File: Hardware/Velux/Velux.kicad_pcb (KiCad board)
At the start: 2 copper layers, 67 x 62 mm, 24 parts, among them J1 5VIN, J2 Conn_01x02_Female, J3 Velux_OUT, J4 24V_IN, J5 FLASH, K1 UMS05-1A80-75L, K2 SANYOU_SRD_Form_C, K3 SANYOU_SRD_Form_C, SW1 RESET, SW2 FLASH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

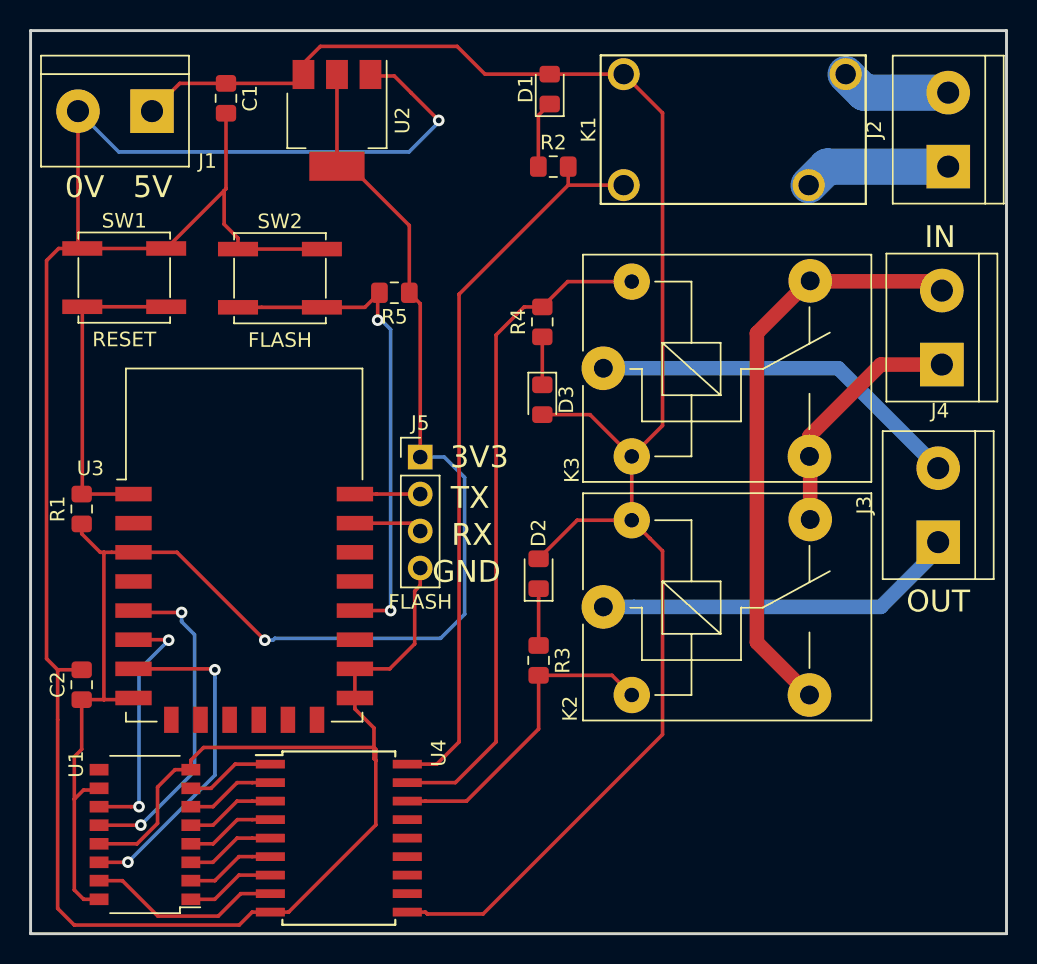
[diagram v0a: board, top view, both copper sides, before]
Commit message: - Modified almost all hardware boards : They were missing a pull-up resistor on GPIO2, which made impossible to flash. - Updated baseBoard.* files
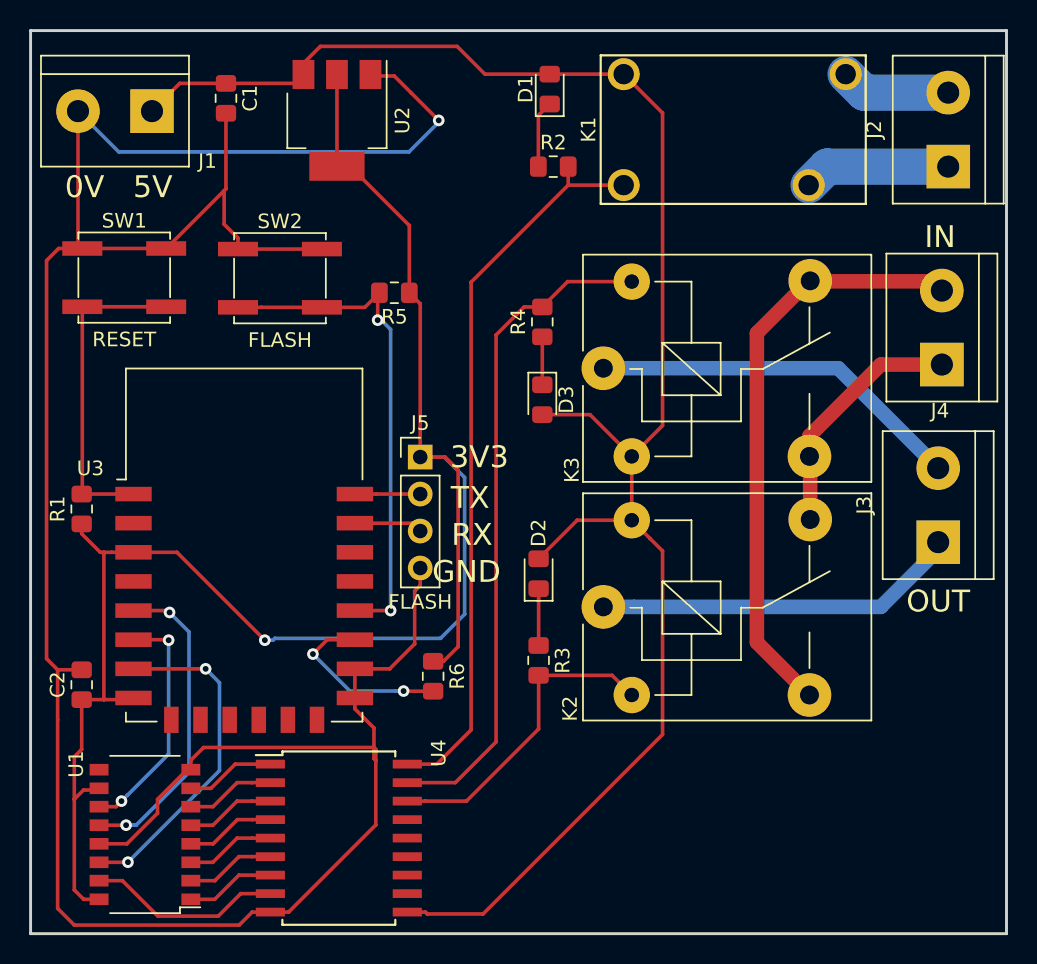
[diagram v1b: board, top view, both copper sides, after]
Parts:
- added R6: 10K, Resistor_SMD:R_0805_2012Metric_Pad1.15x1.40mm_HandSolder, F.Cu at (159.6, 88.3)
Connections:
- U1 pad 9: Net-(U1-Pad9) -> (no net)
- U3 pad 10: Net-(U3-Pad10) -> (no net)
- U3 pad 11: Net-(U3-Pad11) -> (no net)
- U3 pad 12: Net-(U3-Pad12) -> (no net)
- U3 pad 13: Net-(U3-Pad13) -> (no net)
- U3 pad 14: Net-(U3-Pad14) -> (no net)
- U3 pad 19: Net-(U3-Pad19) -> (no net)
- U3 pad 2: Net-(U3-Pad2) -> (no net)
- U3 pad 20: Net-(U3-Pad20) -> (no net)
- U3 pad 4: Net-(U3-Pad4) -> (no net)
- U3 pad 9: Net-(U3-Pad9) -> (no net)
- U4 pad 11: Net-(U4-Pad11) -> (no net)
- U4 pad 12: Net-(U4-Pad12) -> (no net)
- U4 pad 13: Net-(U4-Pad13) -> (no net)
- U4 pad 14: Net-(U4-Pad14) -> (no net)
- U4 pad 15: Net-(U4-Pad15) -> (no net)
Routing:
- net /3V3: track 103.9 -> 121.1 mm
- net Net-(R6-Pad2): track 0.00 -> 12.6 mm, vias 0 -> 2
- net /RCLK: track 22.7 -> 21.7 mm
- net /SRCLK: track 17.4 -> 16.5 mm
- net /GND: track 189.6 -> 188.7 mm
